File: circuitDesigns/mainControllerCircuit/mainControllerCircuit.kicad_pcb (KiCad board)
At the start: 2 copper layers, 125 x 99.8 mm, 49 parts, among them J1 USB_A, J2 USB_A, J3 USB_A, J4 Conn_01x15_Pin, J5 Conn_01x15_Pin, J6 OutputSignals, J7 OutputVCC, Q1 AO3400A, Q10 AO3400A, Q11 AO3400A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

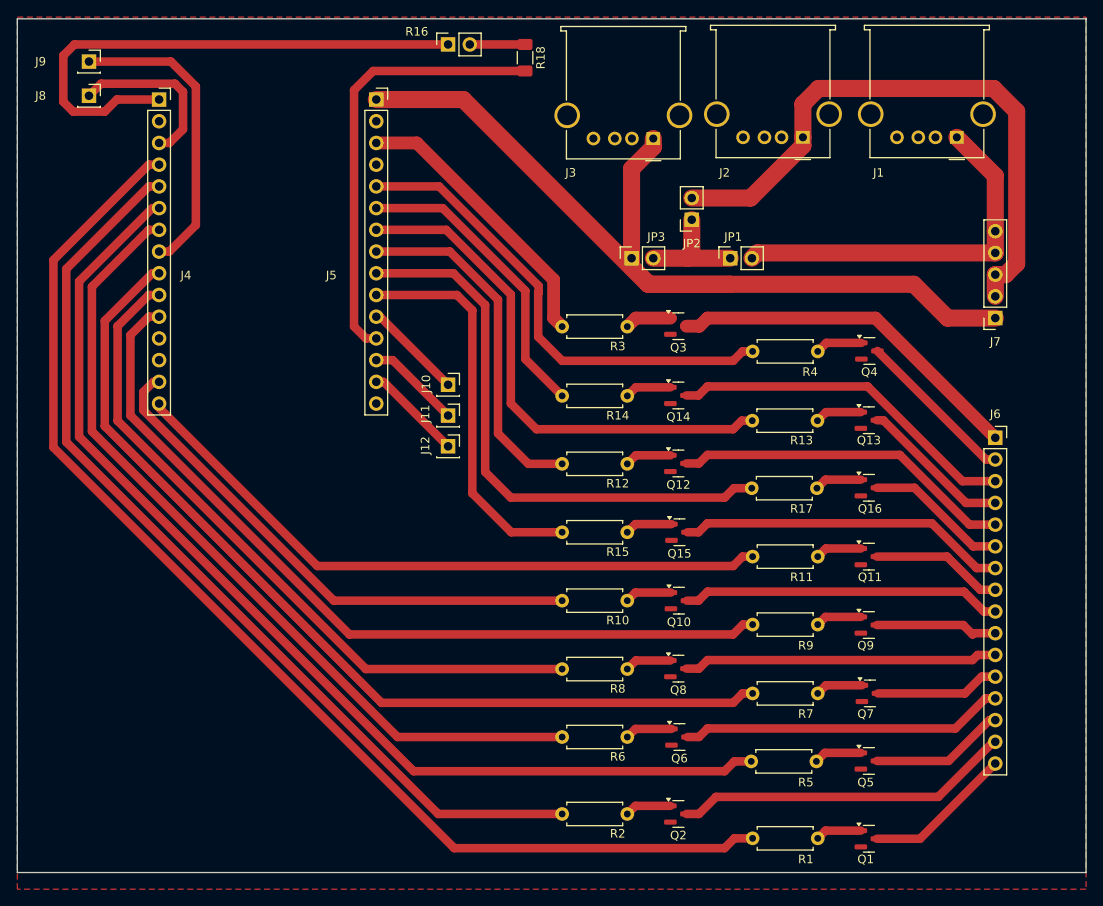
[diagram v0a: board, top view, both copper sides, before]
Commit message: Updates design files for main controller to better accomodate to manufacturer specs
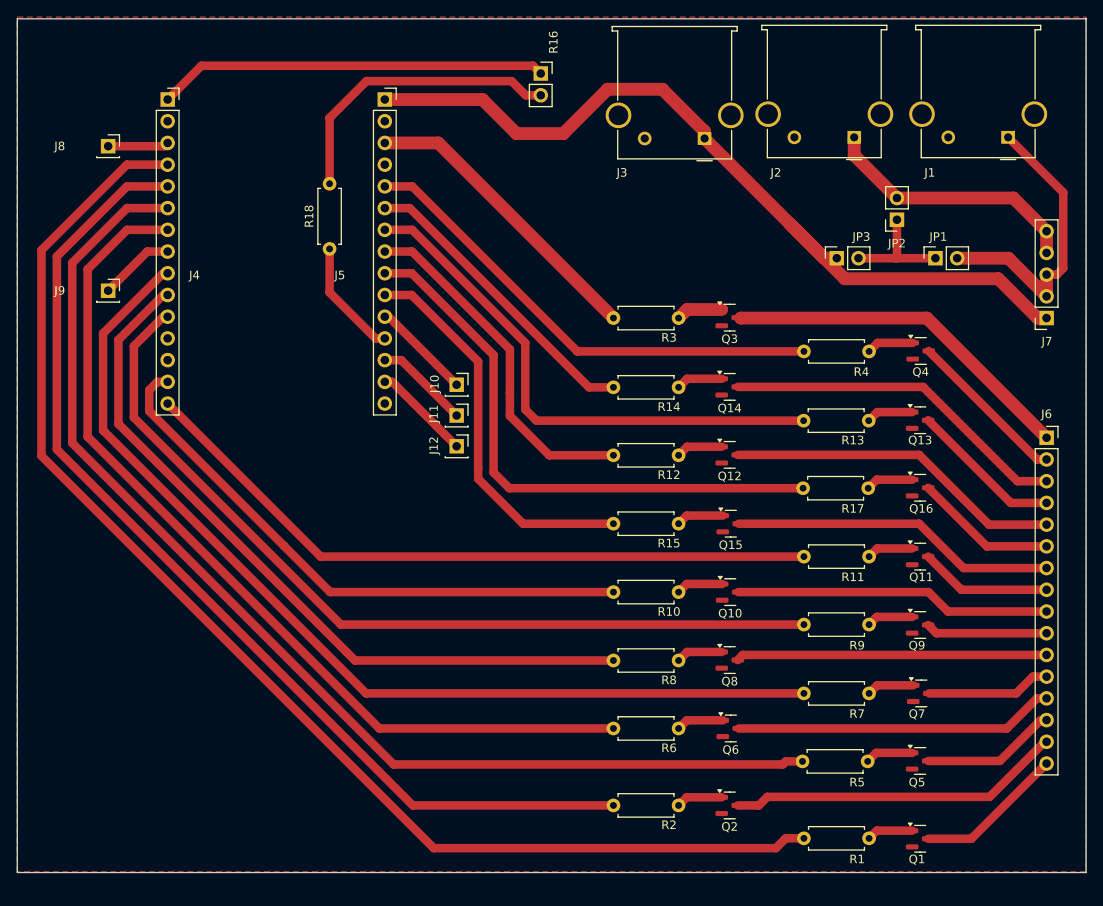
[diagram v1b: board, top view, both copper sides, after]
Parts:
- J6: value OutputSignals -> Conn_01x16_Socket
- R18: footprint Resistor_SMD:R_1206_3216Metric_Pad1.30x1.75mm_HandSolder -> Resistor_THT:R_Axial_DIN0207_L6.3mm_D2.5mm_P7.62mm_Horizontal
- moved R18 32.0 mm to (188.8, 46.9)
- moved J9 26.9 mm to (162.9, 51.8)
- moved JP1 24.0 mm to (259.7, 48.0)
- moved JP2 24.0 mm to (255.2, 43.5)
- moved JP3 24.0 mm to (248.1, 48.0)
- moved R16 11.4 mm to (213.5, 26.4), turned to 0 degrees
- moved J8 6.31 mm to (162.9, 34.9)
- moved Q10 6.08 mm to (235.7, 87.0)
- moved Q12 6.08 mm to (235.6, 71.0)
- moved Q14 6.08 mm to (235.6, 63.1)
- moved Q15 6.08 mm to (235.7, 79.0)
- moved Q2 6.08 mm to (235.6, 112.0)
- moved Q3 6.08 mm to (235.6, 55.0)
- moved Q6 6.08 mm to (235.7, 103.0)
- moved Q8 6.08 mm to (235.6, 95.0)
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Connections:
- J7 pad 2: Net-(J2-VBUS) -> Net-(J1-VBUS)
- J7 pad 3: Net-(J2-VBUS) -> Net-(J1-VBUS)
- J7 pad 4: Net-(J1-VBUS) -> Net-(J2-VBUS)
- J7 pad 5: Net-(J1-VBUS) -> Net-(J2-VBUS)
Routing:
- net Net-(J2-VBUS): track 70.6 -> 30.8 mm
- net Net-(J5-Pin_12): track 51.8 -> 13.8 mm
- net Net-(R16-Pad2): track 6.46 -> 34.9 mm
- net Net-(J4-Pin_8): track 35.5 -> 8.86 mm
- net Net-(J4-Pin_1): track 63.2 -> 45.7 mm
- net Net-(J4-Pin_3): track 19.8 -> 7.12 mm
- net +5V: track 111.4 -> 99.9 mm
- net Net-(J4-Pin_4): track 140.6 -> 151.6 mm
- net Net-(J4-Pin_5): track 111.1 -> 121.3 mm
- net Net-(J4-Pin_6): track 126.4 -> 136.0 mm
- net Net-(J4-Pin_7): track 97.3 -> 106.5 mm
- net Net-(J1-VBUS): track 44.1 -> 35.1 mm
- net Net-(J4-Pin_9): track 110.6 -> 116.5 mm
- net Net-(J4-Pin_10): track 81.4 -> 87.1 mm
- net Net-(J4-Pin_14): track 62.7 -> 68.1 mm
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
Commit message: Increases clearances between the pads to not have a safer margin above the minimum limits of the manufacturer
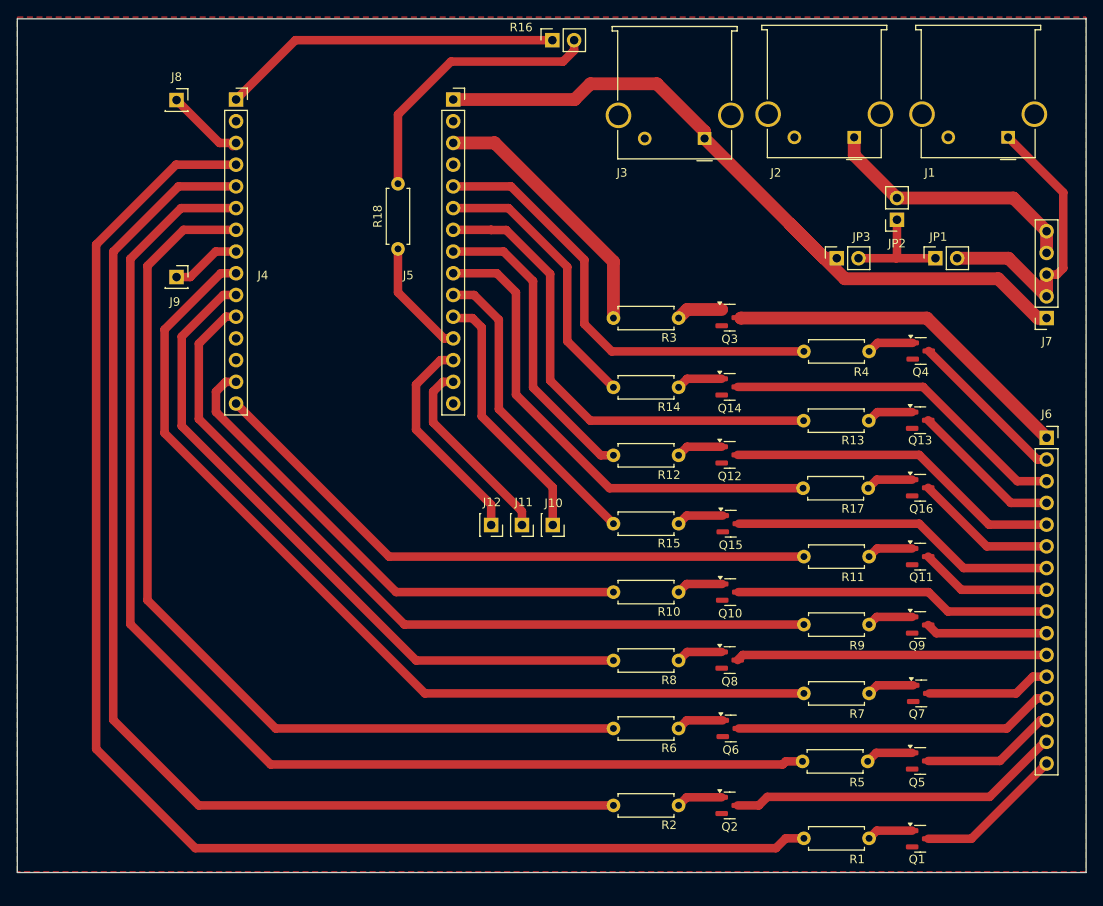
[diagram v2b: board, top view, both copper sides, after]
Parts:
- moved J10 19.9 mm to (214.9, 79.2), turned to -90 degrees
- moved J11 14.9 mm to (211.3, 79.2), turned to -90 degrees
- moved J12 10.0 mm to (207.7, 79.2), turned to -90 degrees
- moved J8 9.65 mm to (170.9, 29.5)
- moved J9 8.16 mm to (170.9, 50.2)
- moved J4 8.00 mm to (177.9, 29.4)
- moved J5 8.00 mm to (203.3, 29.4)
- moved R18 8.00 mm to (196.8, 46.9)
- moved R16 4.13 mm to (214.9, 22.5), turned to 90 degrees
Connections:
- J5 pad 13: Net-(J11-Pin_1) -> Net-(J12-Pin_1)
- J5 pad 14: Net-(J12-Pin_1) -> Net-(J11-Pin_1)
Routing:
- net Net-(J10-Pin_1): track 11.7 -> 30.4 mm
- net Net-(J4-Pin_4): track 151.6 -> 167.3 mm
- net Net-(J12-Pin_1): track 11.5 -> 25.6 mm
- net Net-(J4-Pin_5): track 121.3 -> 134.9 mm
- net Net-(J11-Pin_1): track 11.1 -> 22.7 mm
- net +5V: track 99.9 -> 89.1 mm
- net Net-(J5-Pin_10): track 45.9 -> 35.9 mm
- net Net-(J5-Pin_9): track 67.4 -> 58.3 mm
- net Net-(J4-Pin_15): track 81.8 -> 73.8 mm
- net Net-(J4-Pin_14): track 68.1 -> 60.4 mm
- net Net-(J4-Pin_6): track 136.0 -> 143.1 mm
- net Net-(J4-Pin_11): track 102.1 -> 95.2 mm
- net Net-(J4-Pin_10): track 87.1 -> 80.7 mm
- net Net-(J4-Pin_9): track 116.5 -> 110.6 mm
- net Net-(J4-Pin_1): track 45.7 -> 40.0 mm
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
